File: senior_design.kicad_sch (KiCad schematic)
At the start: 0 parts

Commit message: Setup Hierarchical Schematic
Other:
- added sheet Hall Effect (hall_effect.kicad_sch)
- added sheet MCU (mcu.kicad_sch)
- added sheet Memory (memory.kicad_sch)
- added sheet Peripherals (peripherals.kicad_sch)
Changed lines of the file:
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@@
 	(generator_version "9.0")
 	(paper "A4")
+	(sheet
+		(at 63.5 38.1)
+		(size 38.1 25.4)
+		(exclude_from_sim no)
+		(in_bom yes)
+		(on_board yes)
+		(dnp no)
+		(fields_autoplaced yes)
+		(stroke
+			(width 0.1524)
+			(type solid)
+		)
+		(fill
+			(color 0 0 0 0.0000)
+		)
+		(property "Sheetname" "MCU"
+			(at 63.5 37.3884 0)
+			(effects
+				(font
+					(size 1.27 1.27)
+				)
+				(justify left bottom)
+			)
+		)
+		(property "Sheetfile" "mcu.kicad_sch"
+			(at 63.5 64.0846 0)
+			(effects
+				(font
+					(size 1.27 1.27)
+				)
+				(justify left top)
+			)
+		)
+		(instances
+			(project "senior_design"
+				(path "/35c074f0-8545-4dc1-a57d-3ef0bc7d9188"
+					(page "2")
+				)
+			)
+		)
+	)
+	(sheet
+		(at 139.7 38.1)
+		(size 38.1 24.13)
+		(exclude_from_sim no)
+		(in_bom yes)
+		(on_board yes)
+		(dnp no)
+		(fields_autoplaced yes)
+		(stroke
+			(width 0.1524)
+			(type solid)
+		)
+		(fill
+			(color 0 0 0 0.0000)
+		)
+		(property "Sheetname" "Memory"
+			(at 139.7 37.3884 0)
+			(effects
+				(font
+					(size 1.27 1.27)
+				)
+				(justify left bottom)
+			)
+		)
+		(property "Sheetfile" "memory.kicad_sch"
+			(at 139.7 62.8146 0)
+			(effects
+				(font
+					(size 1.27 1.27)
+				)
+				(justify left top)
+			)
+		)
+		(instances
+			(project "senior_design"
+				(path "/35c074f0-8545-4dc1-a57d-3ef0bc7d9188"
+					(page "4")
+				)
+			)
+		)
+	)
+	(sheet
+		(at 63.5 88.9)
+		(size 38.1 24.13)
+		(exclude_from_sim no)
+		(in_bom yes)
+		(on_board yes)
+		(dnp no)
+		(fields_autoplaced yes)
+		(stroke
+			(width 0.1524)
+			(type solid)
+		)
+		(fill
+			(color 0 0 0 0.0000)
+		)
+		(property "Sheetname" "Hall Effect"
+			(at 63.5 88.1884 0)
+			(effects
+				(font
+					(size 1.27 1.27)
+				)
+				(justify left bottom)
+			)
+		)
+		(property "Sheetfile" "hall_effect.kicad_sch"
+			(at 63.5 113.6146 0)
+			(effects
+				(font
+					(size 1.27 1.27)
+				)
+				(justify left top)
+			)
+		)
+		(instances
+			(project "senior_design"
+				(path "/35c074f0-8545-4dc1-a57d-3ef0bc7d9188"
+					(page "3")
+				)
+			)
+		)
+	)
+	(sheet
+		(at 139.7 88.9)
+		(size 36.83 25.4)
+		(exclude_from_sim no)
+		(in_bom yes)
+		(on_board yes)
+		(dnp no)
+		(fields_autoplaced yes)
+		(stroke
+			(width 0.1524)
+			(type solid)
+		)
+		(fill
+			(color 0 0 0 0.0000)
+		)
+		(property "Sheetname" "Peripherals"
+			(at 139.7 88.1884 0)
+			(effects
+				(font
+					(size 1.27 1.27)
+				)
+				(justify left bottom)
+			)
+		)
+		(property "Sheetfile" "peripherals.kicad_sch"
+			(at 139.7 114.8846 0)
+			(effects
+				(font
+					(size 1.27 1.27)
+				)
+				(justify left top)
+			)
+		)
+		(instances
+			(project "senior_design"
+				(path "/35c074f0-8545-4dc1-a57d-3ef0bc7d9188"
+					(page "5")
+				)
+			)
+		)
+	)
 	(sheet_instances
 		(path "/"

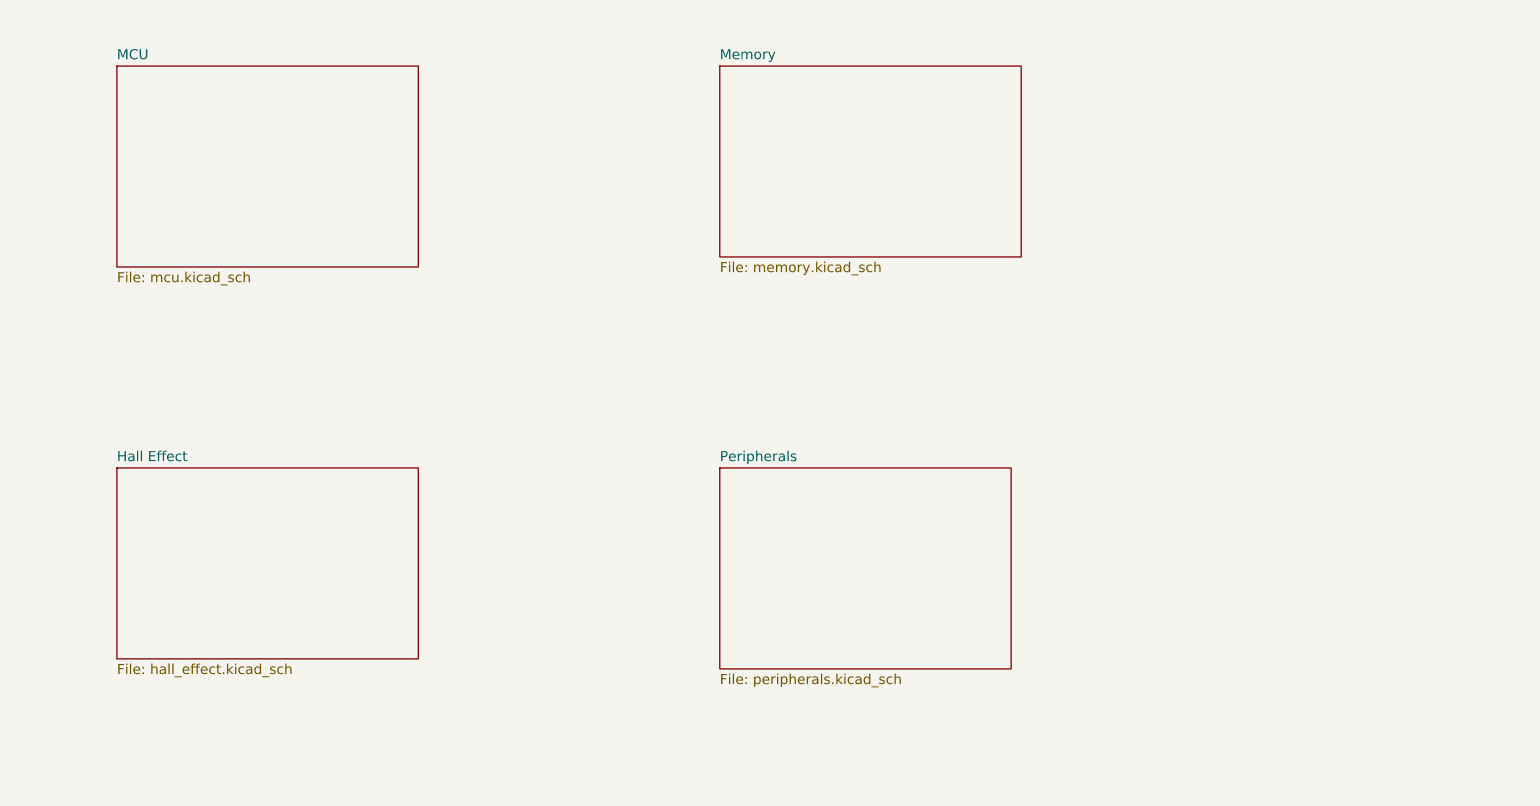
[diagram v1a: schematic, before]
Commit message: added power schematic
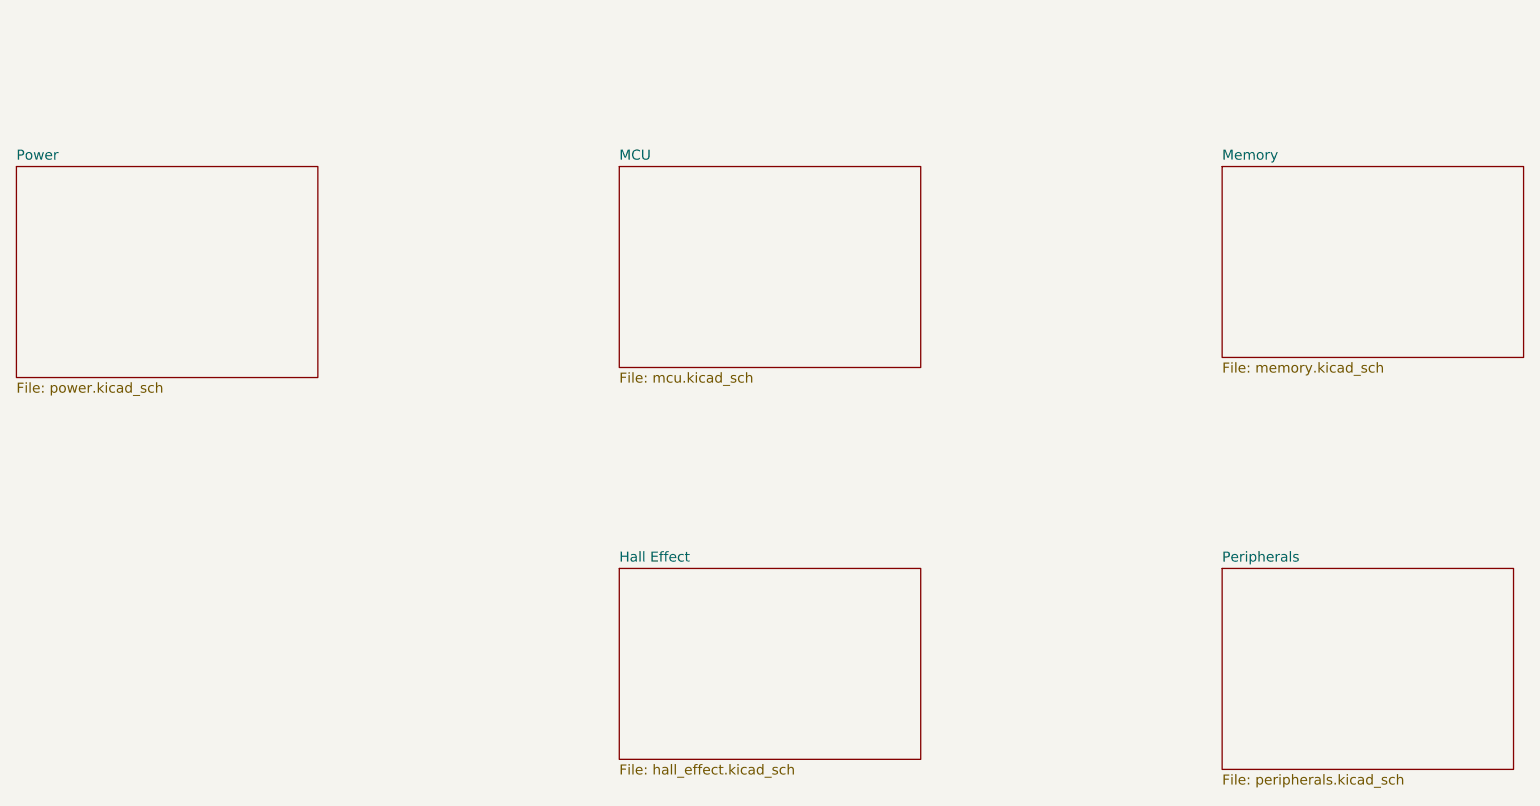
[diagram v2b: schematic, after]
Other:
- added sheet Power (power.kicad_sch)
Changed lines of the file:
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@@
 	(paper "A4")
 	(sheet
-		(at 63.5 38.1)
+		(at 127 50.8)
 		(size 38.1 25.4)
 		(exclude_from_sim no)
@@
 		)
 		(property "Sheetname" "MCU"
-			(at 63.5 37.3884 0)
+			(at 127 50.0884 0)
 			(effects
 				(font
@@
 		)
 		(property "Sheetfile" "mcu.kicad_sch"
-			(at 63.5 64.0846 0)
+			(at 127 76.7846 0)
 			(effects
 				(font
@@
 	)
 	(sheet
-		(at 139.7 38.1)
+		(at 50.8 50.8)
+		(size 38.1 26.67)
+		(exclude_from_sim no)
+		(in_bom yes)
+		(on_board yes)
+		(dnp no)
+		(fields_autoplaced yes)
+		(stroke
+			(width 0.1524)
+			(type solid)
+		)
+		(fill
+			(color 0 0 0 0.0000)
+		)
+		(property "Sheetname" "Power"
+			(at 50.8 50.0884 0)
+			(effects
+				(font
+					(size 1.27 1.27)
+				)
+				(justify left bottom)
+			)
+		)
+		(property "Sheetfile" "power.kicad_sch"
+			(at 50.8 78.0546 0)
+			(effects
+				(font
+					(size 1.27 1.27)
+				)
+				(justify left top)
+			)
+		)
+		(instances
+			(project "senior_design"
+				(path "/35c074f0-8545-4dc1-a57d-3ef0bc7d9188"
+					(page "6")
+				)
+			)
+		)
+	)
+	(sheet
+		(at 203.2 50.8)
 		(size 38.1 24.13)
 		(exclude_from_sim no)
@@
 		)
 		(property "Sheetname" "Memory"
-			(at 139.7 37.3884 0)
+			(at 203.2 50.0884 0)
 			(effects
 				(font
@@
 		)
 		(property "Sheetfile" "memory.kicad_sch"
-			(at 139.7 62.8146 0)
+			(at 203.2 75.5146 0)
 			(effects
 				(font
@@
 	)
 	(sheet
-		(at 63.5 88.9)
+		(at 127 101.6)
 		(size 38.1 24.13)
 		(exclude_from_sim no)
@@
 		)
 		(property "Sheetname" "Hall Effect"
-			(at 63.5 88.1884 0)
+			(at 127 100.8884 0)
 			(effects
 				(font
@@
 		)
 		(property "Sheetfile" "hall_effect.kicad_sch"
-			(at 63.5 113.6146 0)
+			(at 127 126.3146 0)
 			(effects
 				(font
@@
 	)
 	(sheet
-		(at 139.7 88.9)
+		(at 203.2 101.6)
 		(size 36.83 25.4)
 		(exclude_from_sim no)
@@
 		)
 		(property "Sheetname" "Peripherals"
-			(at 139.7 88.1884 0)
+			(at 203.2 100.8884 0)
 			(effects
 				(font
@@
 		)
 		(property "Sheetfile" "peripherals.kicad_sch"
-			(at 139.7 114.8846 0)
+			(at 203.2 127.5846 0)
 			(effects
 				(font

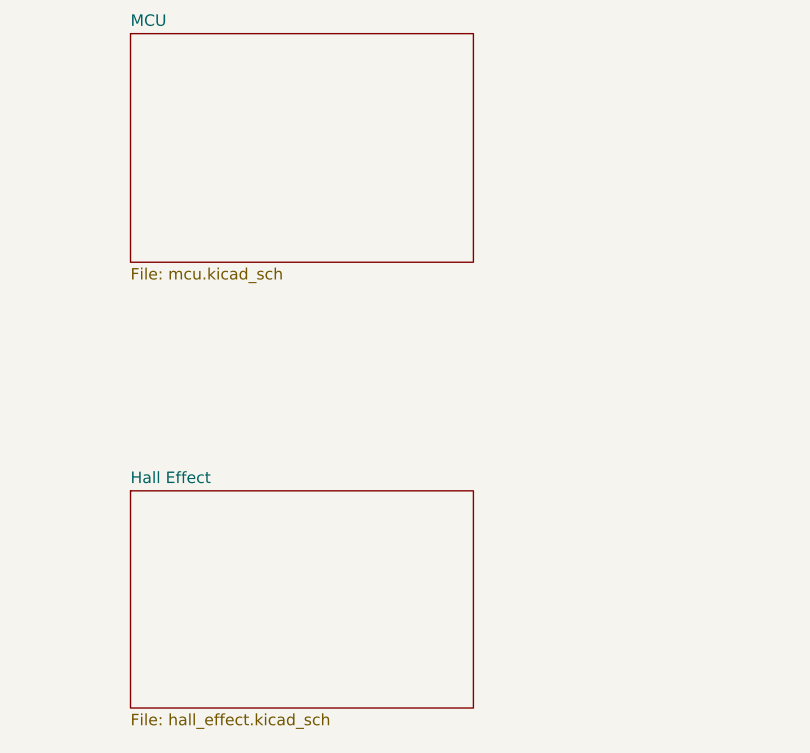
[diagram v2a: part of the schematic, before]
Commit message: added MCU decaps and hall effect schematic
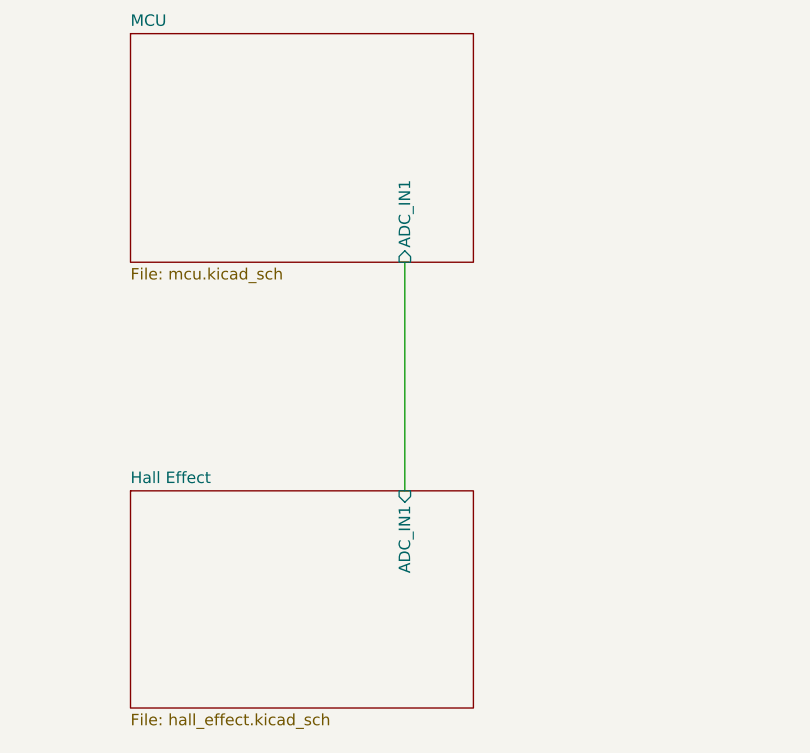
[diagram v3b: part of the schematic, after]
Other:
- sheet Hall Effect ports: added ADC_IN1; removed none
- sheet MCU ports: added ADC_IN1; removed none
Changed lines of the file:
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@@
 	(generator_version "9.0")
 	(paper "A4")
+	(wire
+		(pts
+			(xy 157.48 76.2) (xy 157.48 101.6)
+		)
+		(stroke
+			(width 0)
+			(type default)
+		)
+	)
 	(sheet
 		(at 127 50.8)
@@
 				)
 				(justify left top)
+			)
+		)
+		(pin "ADC_IN1" input
+			(at 157.48 76.2 270)
+			(effects
+				(font
+					(size 1.27 1.27)
+				)
+				(justify left)
 			)
 		)
@@
 			)
 		)
+		(pin "ADC_IN1" input
+			(at 157.48 101.6 90)
+			(effects
+				(font
+					(size 1.27 1.27)
+				)
+				(justify right)
+			)
+		)

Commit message: schematic finish
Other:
- sheet MCU ports: added CS, INT, MISO, MOSI, RST, SCK, WAIT; removed none
- sheet Peripherals ports: added BACKLITE, CS, INT, MISO, MOSI, RESET, SCK, WAIT; removed none

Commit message: Updated Audio Schematic & PCB
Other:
- added sheet Audio (audio.kicad_sch)
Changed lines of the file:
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@@
+	)
+	(sheet
+		(at 50.8 101.6)
+		(size 38.1 25.4)
+		(exclude_from_sim no)
+		(in_bom yes)
+		(on_board yes)
+		(dnp no)
+		(fields_autoplaced yes)
+		(stroke
+			(width 0.1524)
+			(type solid)
+		)
+		(fill
+			(color 0 0 0 0.0000)
+		)
+		(property "Sheetname" "Audio"
+			(at 50.8 100.8884 0)
+			(effects
+				(font
+					(size 1.27 1.27)
+				)
+				(justify left bottom)
+			)
+		)
+		(property "Sheetfile" "audio.kicad_sch"
+			(at 50.8 127.5846 0)
+			(effects
+				(font
+					(size 1.27 1.27)
+				)
+				(justify left top)
+			)
+		)
+		(instances
+			(project "senior_design"
+				(path "/35c074f0-8545-4dc1-a57d-3ef0bc7d9188"
+					(page "7")
+				)
+			)
+		)
 	)
 	(sheet

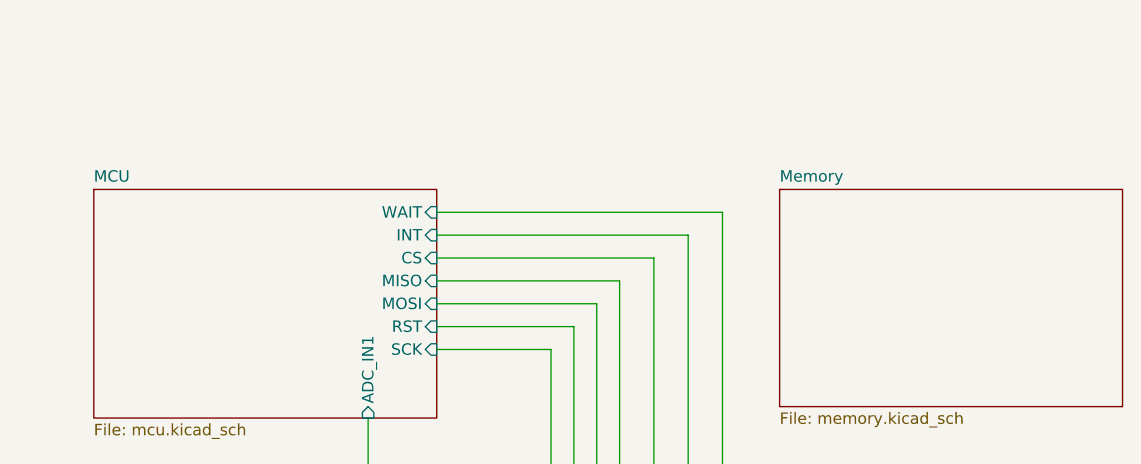
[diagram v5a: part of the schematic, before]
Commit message: added memory and fixed clock
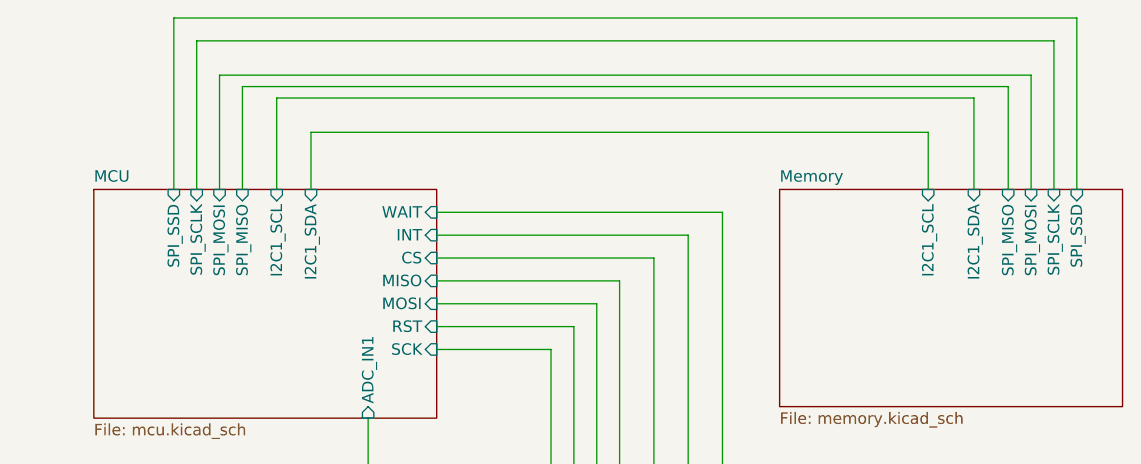
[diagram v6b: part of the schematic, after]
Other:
- sheet MCU ports: added I2C1_SCL, I2C1_SDA, SPI_MISO, SPI_MOSI, SPI_SCLK, SPI_SSD; removed none
- sheet Memory ports: added I2C1_SCL, I2C1_SDA, SPI_MISO, SPI_MOSI, SPI_SCLK, SPI_SSD; removed none

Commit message: Updated Schematic
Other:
- sheet Audio ports: added AUDIO_IN; removed none
- sheet MCU ports: added AUDIO_OUT; removed none
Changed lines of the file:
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@@
+	(wire
+		(pts
+			(xy 109.22 106.68) (xy 109.22 71.12)
+		)
+		(stroke
+			(width 0)
+			(type default)
+		)
+	)
 	(wire
 		(pts
@@
 	(wire
 		(pts
+			(xy 88.9 106.68) (xy 109.22 106.68)
+		)
+		(stroke
+			(width 0)
+			(type default)
+		)
+	)
+	(wire
+		(pts
 			(xy 147.32 50.8) (xy 147.32 40.64)
 		)
@@
 		(pts
 			(xy 189.23 58.42) (xy 189.23 113.03)
+		)
+		(stroke
+			(width 0)
+			(type default)
+		)
+	)
+	(wire
+		(pts
+			(xy 109.22 71.12) (xy 127 71.12)
 		)
 		(stroke
@@
 			)
 		)
+		(pin "AUDIO_OUT" input
+			(at 127 71.12 180)
+			(effects
+				(font
+					(size 1.27 1.27)
+				)
+				(justify left)
+			)
+		)
 		(instances
 			(project "senior_design"
@@
 			)
 		)
+		(pin "AUDIO_IN" input
+			(at 88.9 106.68 0)
+			(effects
+				(font
+					(size 1.27 1.27)
+				)
+				(justify right)
+			)
+		)

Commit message: Updated Schematic
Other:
- sheet Hall Effect ports: added VDDA; removed none
- sheet MCU ports: added VDDA; removed none
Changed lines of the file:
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@@
+	(wire
+		(pts
+			(xy 147.32 76.2) (xy 147.32 101.6)
+		)
+		(stroke
+			(width 0)
+			(type default)
+		)
+	)
 	(wire
 		(pts
@@
 			)
 		)
+		(pin "VDDA" input
+			(at 147.32 76.2 270)
+			(effects
+				(font
+					(size 1.27 1.27)
+				)
+				(justify left)
+			)
+		)
 		(instances
 			(project "senior_design"
@@
 			(effects
 				(font
+					(size 1.27 1.27)
+				)
+				(justify right)
+			)
+		)
+		(pin "VDDA" input
+			(at 147.32 101.6 90)
+			(effects
+				(font
